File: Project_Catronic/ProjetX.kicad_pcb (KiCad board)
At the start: 4 copper layers, 57 x 54 mm, 99 parts, among them IC1 MP1475DJ-LF-P, J1 Conn_ST_STDC14, J11 Conn_01x05, J2 Screw_Terminal_01x02, J3 Conn_01x06, J4 BORDER, J5 Conn_01x06, J6 Conn_01x05, J7 BORDER, J8 BORDER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

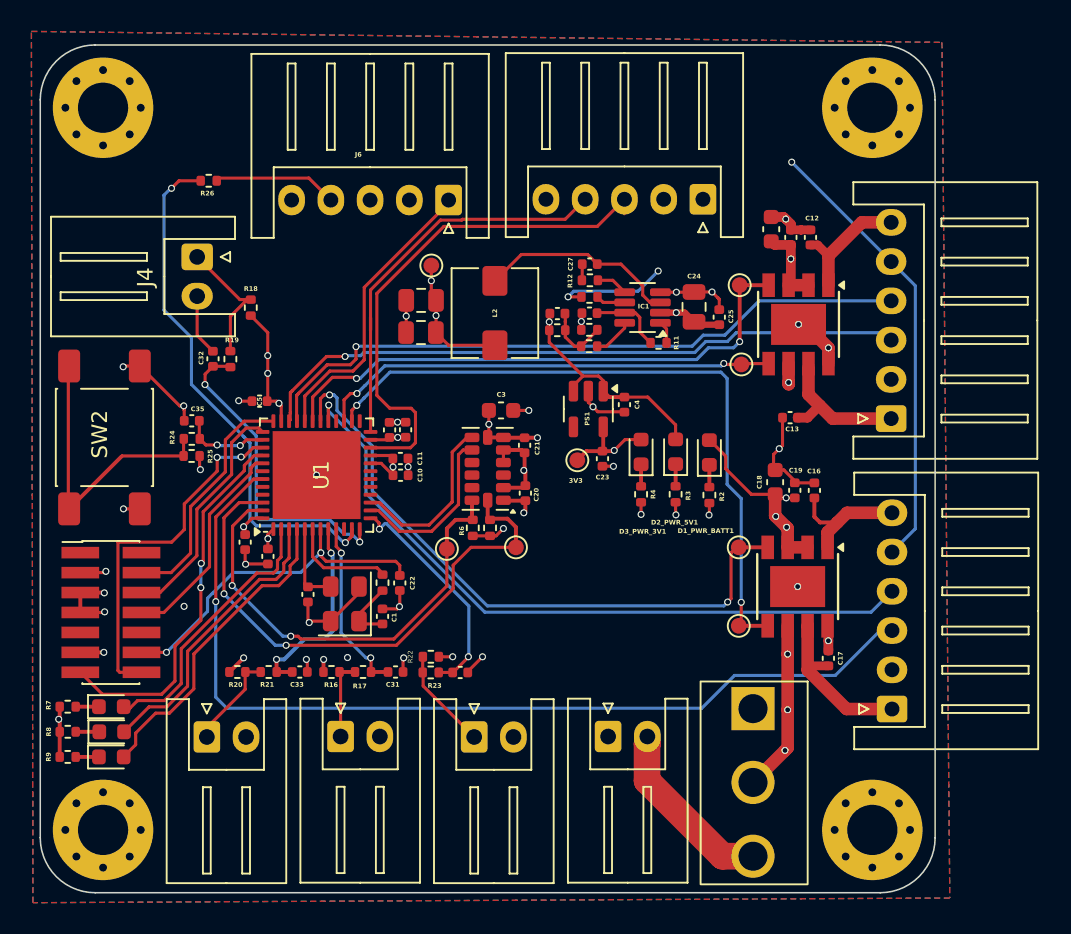
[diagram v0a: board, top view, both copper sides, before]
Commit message: Update KiCad project with latest schematic and PCB edits
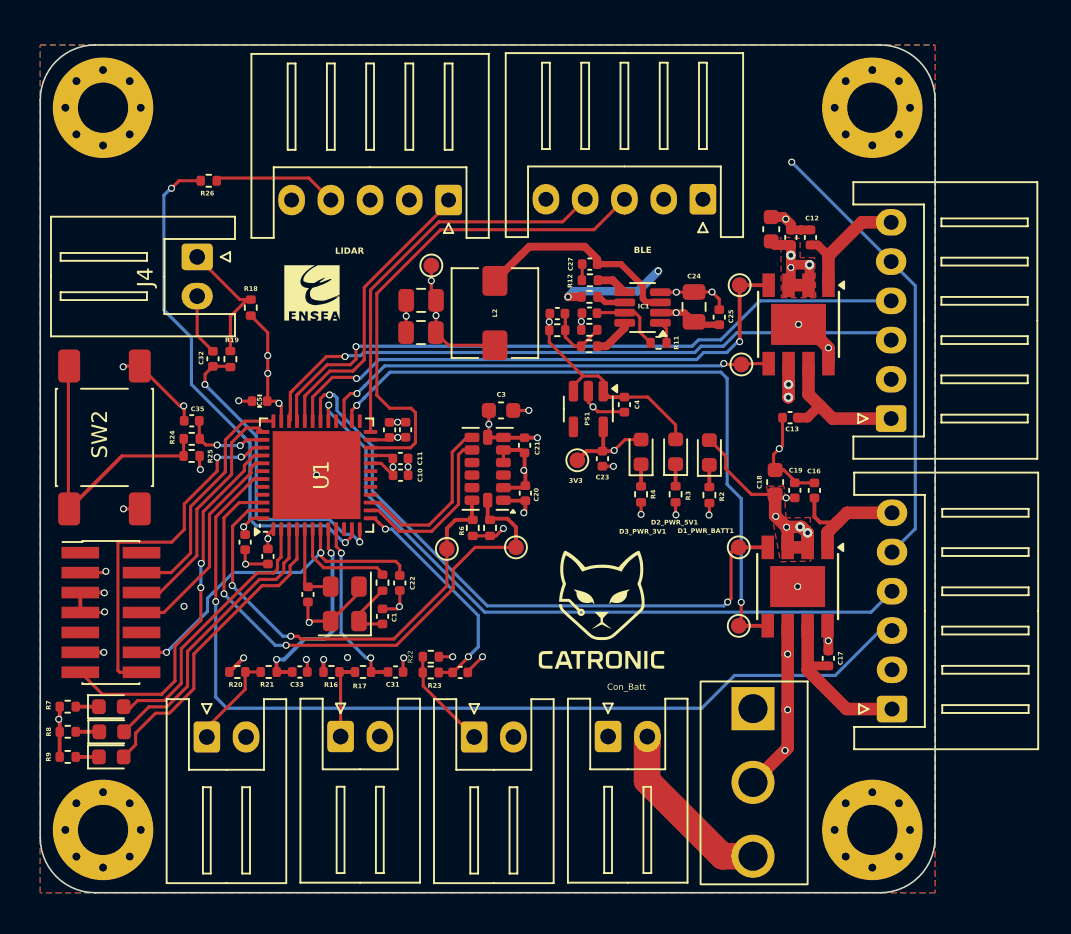
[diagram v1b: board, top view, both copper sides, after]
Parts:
- added G***: LOGO, LOGO, F.Cu at (152.4, 90.6)
- added G***: LOGO, LOGO, F.Cu at (170.8, 111.4)
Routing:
- net +BATT: track 42.1 -> 47.9 mm, vias 11 -> 16
- net Net-(IC1-SW): track 12.8 -> 13.6 mm
- added copper zone on F.Cu, net +BATT
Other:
- board text added: "BLE"
- board text added: "Con_Batt"
- board text added: "LIDAR"
